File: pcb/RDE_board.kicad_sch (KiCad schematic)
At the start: 36 parts, among them J4 7772, J5 7772, J6 7772, J7 7772

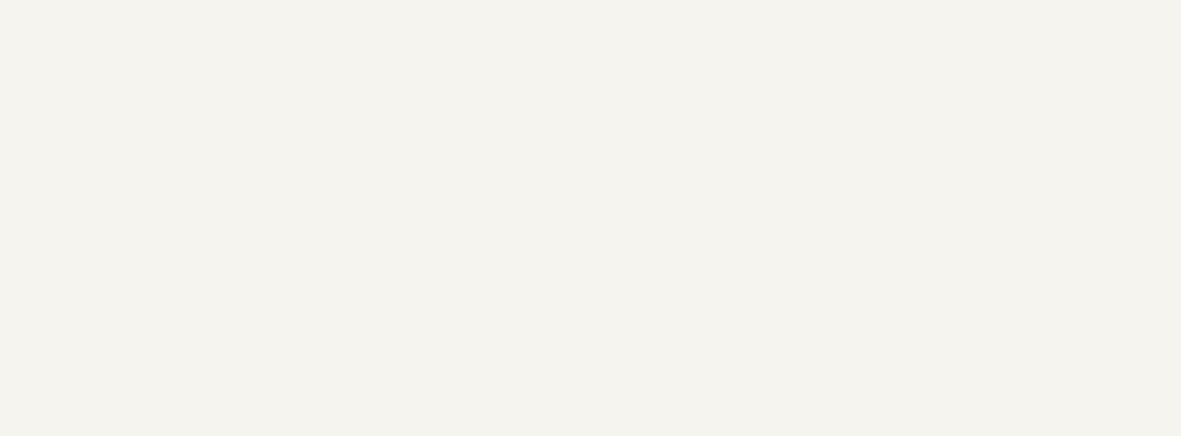
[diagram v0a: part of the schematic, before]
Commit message: Modification based on prototype
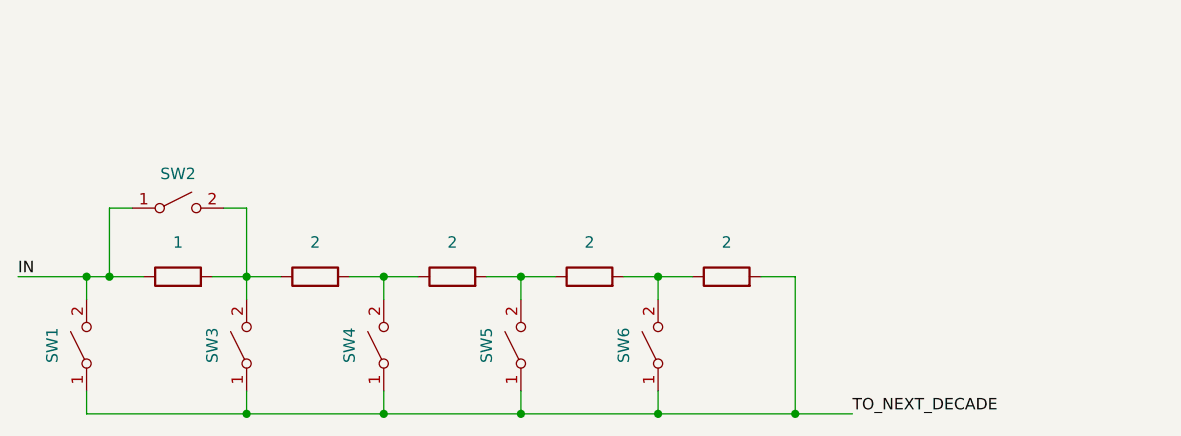
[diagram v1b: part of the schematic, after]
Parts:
- added R92: 1, Resistor_SMD:R_0603_1608Metric_Pad0.98x0.95mm_HandSolder, symbol Device:R
- added R93, R94, R95, R96: 2, Resistor_SMD:R_0603_1608Metric_Pad0.98x0.95mm_HandSolder, symbol Device:R
- added SW1, SW2, SW3, SW4, SW5, SW6: SW_SPST, symbol Switch:SW_SPST
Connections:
- new net: R92.2, R93.1, SW2.2 (B), SW3.2 (B)
- new net: R94.2, R95.1, SW5.2 (B)
- new net: R95.2, R96.1, SW6.2 (B)
- new net: R93.2, R94.1, SW4.2 (B)
- new net IN: R92.1, SW1.2 (B), SW2.1 (A)
- new net TO_NEXT_DECADE: R96.2, SW1.1 (A), SW3.1 (A), SW4.1 (A), SW5.1 (A), SW6.1 (A)
